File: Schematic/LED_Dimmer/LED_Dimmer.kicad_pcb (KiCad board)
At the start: 2 copper layers, 71 x 39 mm, 27 parts, among them J1 From PSU, J2 LED Spots, J3 To microsocope, J4 LED Ring, U1 AL8861Y-13, U2 AL8861Y-13

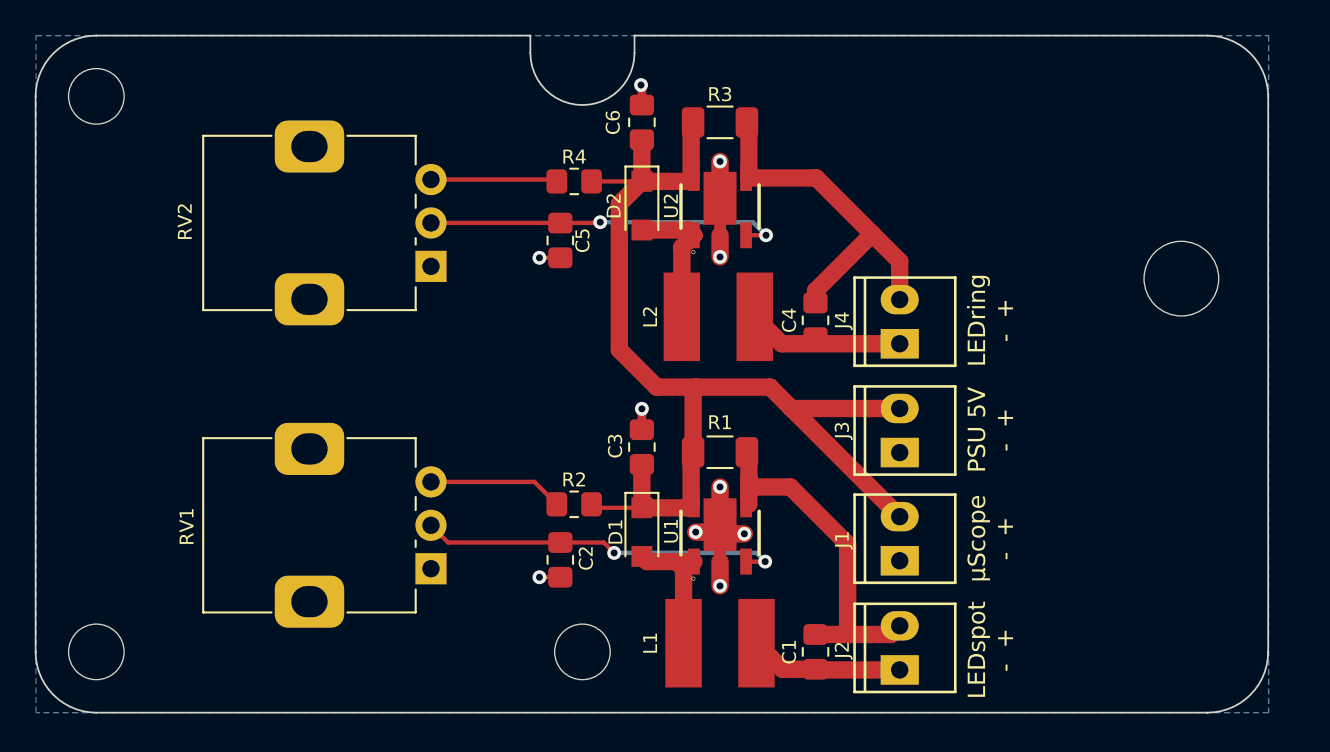
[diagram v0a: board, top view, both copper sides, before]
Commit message: Adjusted mounting hole position
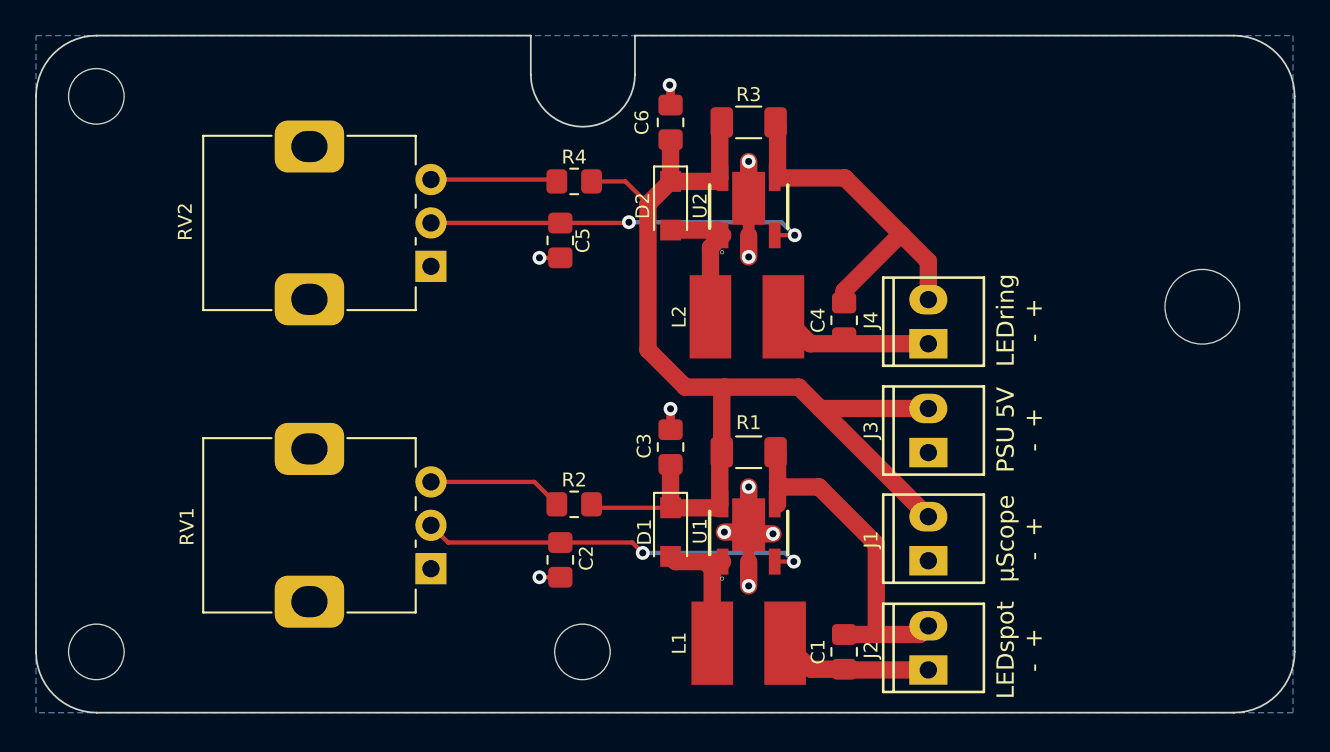
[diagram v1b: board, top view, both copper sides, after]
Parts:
- moved G*** 3.98 mm to (101.3, 35.5)
- moved H4 2.02 mm to (108.2, 49.6)
- moved J1 1.65 mm to (92.4, 63.0)
- moved J2 1.65 mm to (92.4, 69.3)
- moved J3 1.65 mm to (92.4, 56.8)
- moved J4 1.65 mm to (92.4, 50.5)
- moved L2 1.65 mm to (82.0, 50.2)
- moved C1 1.65 mm to (87.5, 69.5)
- moved C3 1.65 mm to (77.5, 57.7)
- moved C4 1.65 mm to (87.5, 50.4)
- moved C6 1.65 mm to (77.5, 39.0)
- moved D1 1.65 mm to (77.5, 62.6)
- moved D2 1.65 mm to (77.5, 43.8)
- moved L1 1.65 mm to (82.0, 69.0)
- moved R1 1.65 mm to (82.0, 58.0)
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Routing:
- net +5V: track 63.3 -> 65.8 mm
- net Net-(U2-VSET): track 20.8 -> 22.4 mm
- net Net-(U1-VSET): track 21.2 -> 22.9 mm
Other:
- board size 71 x 39 mm -> 72.5 x 39 mm
- board text added: "Andonstar_LED_Dimmer R0143B_2331 Bjørner Sandom"
- board text removed: "Andonstar_LED_Dimmer R0143_2329 Bjørner Sandom"

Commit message: New PCB layout
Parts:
- added C5: 22µF, Resistor_SMD:R_0805_2012Metric_Pad1.20x1.40mm_HandSolder, F.Cu at (104.1, 66.0)
- J1: renamed from J2; footprint myDevices:KF2510-2P -> myDevices:KF2510-2P-Angle
- J2: renamed from J1; footprint myDevices:KF2510-2P -> myDevices:KF2510-2P-Angle
- J3: renamed from J4; footprint myDevices:KF2510-2P -> myDevices:KF2510-2P-Angle
- J4: renamed from J3; footprint myDevices:KF2510-2P -> myDevices:KF2510-2P-Angle
- R1: value 200mΩ 0.5W -> 200mΩ 0.25W
- R3: value 200mΩ 0.5W -> 120mΩ 0.25W
- moved J2 32.9 mm to (66.9, 42.2), turned to -90 degrees
- moved R3 19.3 mm to (65.4, 48.8), turned to 90 degrees
- moved C6 19.0 mm to (53.7, 53.3), turned to 180 degrees
- moved C2 18.8 mm to (53.7, 71.0), turned to 180 degrees
- moved C7 18.7 mm to (65.4, 53.3), turned to 180 degrees
- moved R4 17.6 mm to (58.1, 53.3)
- moved R2 17.1 mm to (58.1, 71.0)
- moved R1 16.5 mm to (65.6, 59.3), turned to 90 degrees
- moved J3 16.3 mm to (93.0, 66.7), turned to 0 degrees
- moved C3 13.7 mm to (65.3, 63.8), turned to 180 degrees
- moved U2 12.7 mm to (70.3, 48.8), turned to 90 degrees
- moved J4 12.4 mm to (99.8, 66.7), turned to 0 degrees
- moved U1 12.2 mm to (70.3, 59.3), turned to 90 degrees
- moved RV1 12.1 mm to (52.2, 68.4), turned to 90 degrees
- moved RV2 12.0 mm to (52.2, 50.7), turned to 90 degrees
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- renumbered C5 to C6, C6 to C7
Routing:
- net +5V: track 65.8 -> 112.0 mm
- net Net-(J3-Pin_2): track 21.5 -> 44.4 mm
- net Net-(J3-Pin_1): track 8.99 -> 28.4 mm
- net Net-(J1-Pin_2): track 20.4 -> 31.0 mm
- net Net-(J1-Pin_1): track 8.89 -> 15.2 mm
- net Net-(R2-Pad1): track 7.79 -> 2.60 mm
- net Net-(U1-VSET): track 22.9 -> 27.8 mm, vias 2 -> 1
- net Net-(R4-Pad1): track 7.29 -> 2.68 mm
- net GND: track 14.8 -> 19.3 mm, vias 10 -> 9
- net Net-(U2-VSET): track 22.4 -> 21.3 mm, vias 2 -> 1
- net Net-(D2-A): track 8.11 -> 8.90 mm
- net Net-(D1-A): track 7.99 -> 8.72 mm
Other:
- outline, holes or cut-outs redrawn
- board text added: "Andonstar_LED_Dimmer R0143C_2333 Bjørner Sandom"
- board text added: "PSU 5V + -"
- board text removed: "Andonstar_LED_Dimmer R0143B_2331 Bjørner Sandom"
- board text removed: "PSU 5V - +"
